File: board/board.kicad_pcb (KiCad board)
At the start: 2 copper layers, 21 x 13 mm, 9 parts, among them J1 012_CAN, J2 Conn_01x03_Male, U1 TJA1441

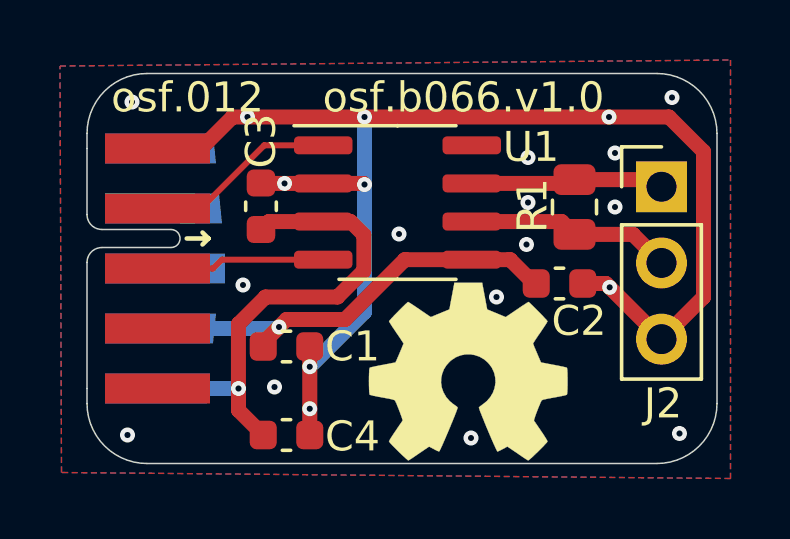
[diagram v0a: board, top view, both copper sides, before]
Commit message: changed transceiver chip to be more availible TJA1044GT version
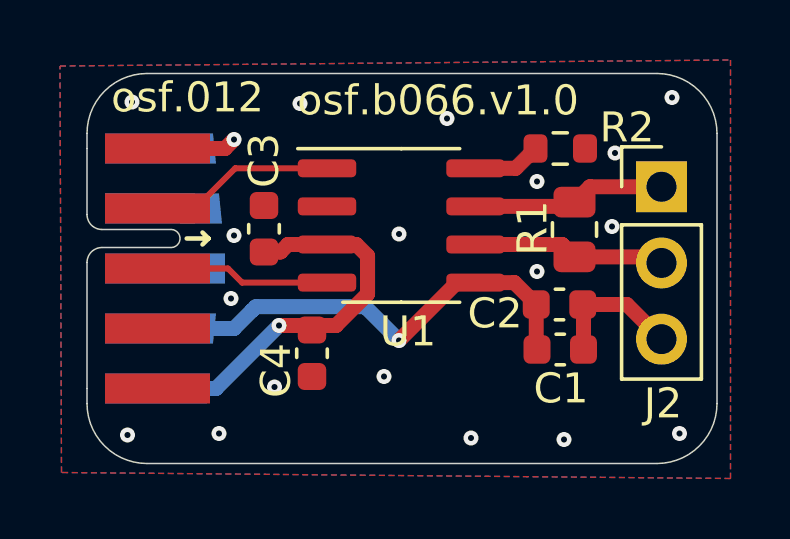
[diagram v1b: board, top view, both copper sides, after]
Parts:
- added R2: 0R, Resistor_SMD:R_0603_1608Metric, F.Cu at (155.8, 92.5)
- LOGO1: moved to B.Cu
- U1: value TJA1441 -> TJA144
- moved C1 9.13 mm to (155.8, 99.2)
- moved LOGO1 3.80 mm to (150.3, 97.0), turned to 180 degrees
- moved C4 2.85 mm to (147.5, 99.3), turned to -90 degrees
- moved U1 0.78 mm to (150.5, 95.1)
- moved C3 0.76 mm to (145.9, 95.2)
- moved R1 0.75 mm to (156.2, 95.2)
- moved C2 0.70 mm to (155.8, 97.7)
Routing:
- net GND: track 44.8 -> 7.29 mm, vias 22 -> 19
- net /transceiver/VDD: track 16.6 -> 13.3 mm
- net /transceiver/STBY: track 0.00 -> 2.27 mm
